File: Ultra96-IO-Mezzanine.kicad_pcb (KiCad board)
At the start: 2 copper layers, 85 x 54 mm, 6 parts, among them P1 CONN_02X20, P2 CONN_02X20

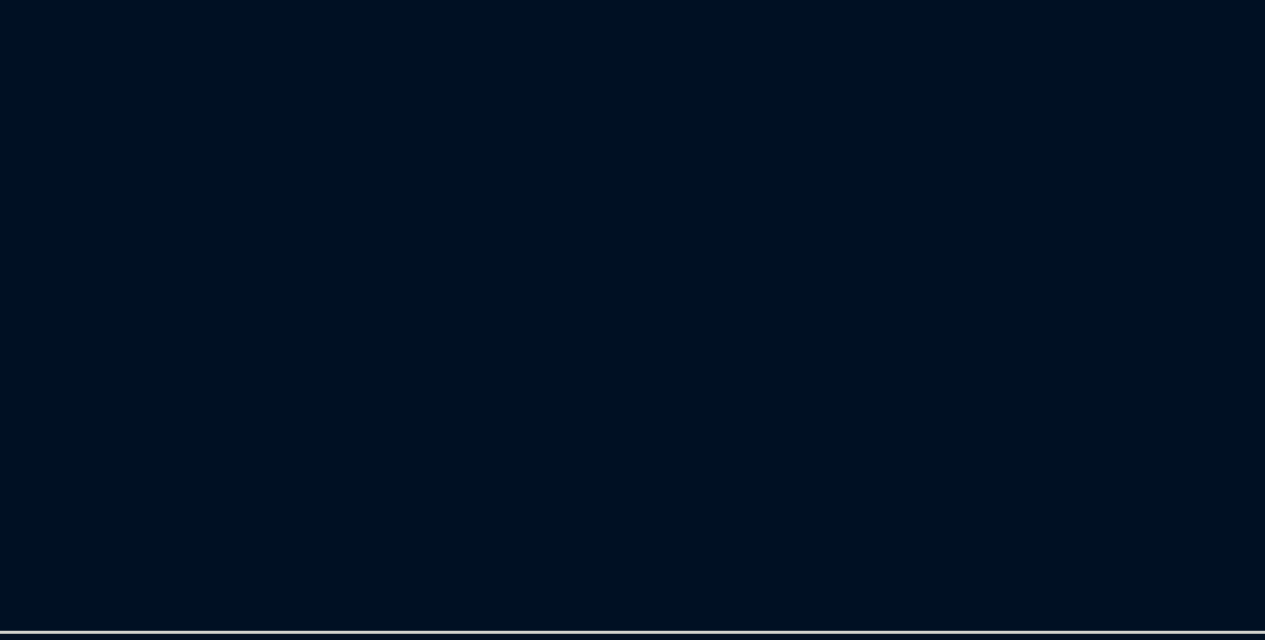
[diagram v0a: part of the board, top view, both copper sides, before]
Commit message: highspeed connector
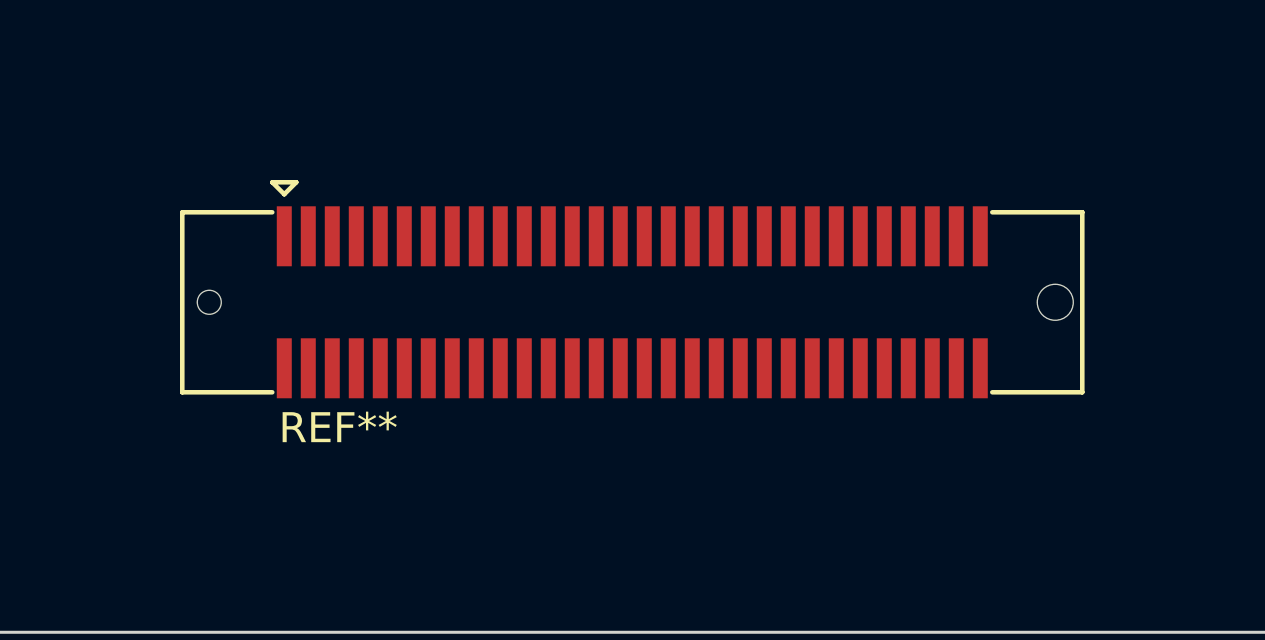
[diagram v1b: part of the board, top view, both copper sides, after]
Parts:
- added REF**: 61083-063400LF, 96board-hs:61083-063400LF, F.Cu at (130.8, 143.0)
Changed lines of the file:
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@@
-(kicad_pcb (version 20171130) (host pcbnew 5.1.6-c6e7f7d~86~ubuntu20.04.1)
+(kicad_pcb (version 20171130) (host pcbnew 5.1.6-c6e7f7d~87~ubuntu20.04.1)
   (general
     (thickness 1.6)
@@
     (tracks 0)
     (zones 0)
-    (modules 6)
+    (modules 7)
     (nets 37)
   )
@@
     (add_net GND)
   )
+  (module 96board-hs:61083-063400LF (layer F.Cu)
+    (at 130.8 143)
+    (fp_text reference REF** (at -9.8 4.2) (layer F.SilkS)
+      (effects (font (size 1 1) (thickness 0.15)))
+    )
+    (fp_text value 61083-063400LF (at -0.2 0) (layer F.Fab)
+      (effects (font (size 1 1) (thickness 0.15)))
+    )
+    (fp_line (start -15 -3) (end -15 3) (layer F.SilkS) (width 0.1524))
+    (fp_line (start 15 -3) (end 15 3) (layer F.SilkS) (width 0.1524))
+    (fp_line (start 15 -3) (end 12 -3) (layer F.SilkS) (width 0.1524))
+    (fp_line (start 15 3) (end 12 3) (layer F.SilkS) (width 0.1524))
+    (fp_line (start -15 3) (end -12 3) (layer F.SilkS) (width 0.1524))
+    (fp_line (start -15 -3) (end -12 -3) (layer F.SilkS) (width 0.1524))
+    (fp_line (start -12 -4) (end -11.6 -3.6) (layer F.SilkS) (width 0.1524))
+    (fp_line (start -11.6 -3.6) (end -11.2 -4) (layer F.SilkS) (width 0.1524))
+    (fp_line (start -11.2 -4) (end -12 -4) (layer F.SilkS) (width 0.1524))
+    (pad 57 smd rect (at 10.8 -2.2) (size 0.5 2) (layers F.Cu F.Paste F.Mask))
+    (pad 54 smd rect (at 9.2 2.2) (size 0.5 2) (layers F.Cu F.Paste F.Mask))
+    (pad 34 smd rect (at 1.2 2.2) (size 0.5 2) (layers F.Cu F.Paste F.Mask))
+    (pad 44 smd rect (at 5.2 2.2) (size 0.5 2) (layers F.Cu F.Paste F.Mask))
+    (pad 43 smd rect (at 5.2 -2.2) (size 0.5 2) (layers F.Cu F.Paste F.Mask))
+    (pad 39 smd rect (at 3.6 -2.2) (size 0.5 2) (layers F.Cu F.Paste F.Mask))
+    (pad 32 smd rect (at 0.4 2.2) (size 0.5 2) (layers F.Cu F.Paste F.Mask))
+    (pad 42 smd rect (at 4.4 2.2) (size 0.5 2) (layers F.Cu F.Paste F.Mask))
+    (pad 40 smd rect (at 3.6 2.2) (size 0.5 2) (layers F.Cu F.Paste F.Mask))
+    (pad 48 smd rect (at 6.8 2.2) (size 0.5 2) (layers F.Cu F.Paste F.Mask))
+    (pad 33 smd rect (at 1.2 -2.2) (size 0.5 2) (layers F.Cu F.Paste F.Mask))
+    (pad 51 smd rect (at 8.4 -2.2) (size 0.5 2) (layers F.Cu F.Paste F.Mask))
+    (pad 41 smd rect (at 4.4 -2.2) (size 0.5 2) (layers F.Cu F.Paste F.Mask))
+    (pad 37 smd rect (at 2.8 -2.2) (size 0.5 2) (layers F.Cu F.Paste F.Mask))
+    (pad 53 smd rect (at 9.2 -2.2) (size 0.5 2) (layers F.Cu F.Paste F.Mask))
+    (pad 35 smd rect (at 2 -2.2) (size 0.5 2) (layers F.Cu F.Paste F.Mask))
+    (pad 38 smd rect (at 2.8 2.2) (size 0.5 2) (layers F.Cu F.Paste F.Mask))
+    (pad 31 smd rect (at 0.4 -2.2) (size 0.5 2) (layers F.Cu F.Paste F.Mask))
+    (pad 58 smd rect (at 10.8 2.2) (size 0.5 2) (layers F.Cu F.Paste F.Mask))
+    (pad 55 smd rect (at 10 -2.2) (size 0.5 2) (layers F.Cu F.Paste F.Mask))
+    (pad 46 smd rect (at 6 2.2) (size 0.5 2) (layers F.Cu F.Paste F.Mask))
+    (pad 45 smd rect (at 6 -2.2) (size 0.5 2) (layers F.Cu F.Paste F.Mask))
+    (pad 49 smd rect (at 7.6 -2.2) (size 0.5 2) (layers F.Cu F.Paste F.Mask))
+    (pad 52 smd rect (at 8.4 2.2) (size 0.5 2) (layers F.Cu F.Paste F.Mask))
+    (pad 60 smd rect (at 11.6 2.2) (size 0.5 2) (layers F.Cu F.Paste F.Mask))
+    (pad 56 smd rect (at 10 2.2) (size 0.5 2) (layers F.Cu F.Paste F.Mask))
+    (pad 50 smd rect (at 7.6 2.2) (size 0.5 2) (layers F.Cu F.Paste F.Mask))
+    (pad 36 smd rect (at 2 2.2) (size 0.5 2) (layers F.Cu F.Paste F.Mask))
+    (pad 59 smd rect (at 11.6 -2.2) (size 0.5 2) (layers F.Cu F.Paste F.Mask))
+    (pad 47 smd rect (at 6.8 -2.2) (size 0.5 2) (layers F.Cu F.Paste F.Mask))
+    (pad "" np_thru_hole circle (at 14.1 0) (size 1.2 1.2) (drill 1.2) (layers *.Cu *.Mask))
+    (pad 1 smd rect (at -11.6 -2.2) (size 0.5 2) (layers F.Cu F.Paste F.Mask))
+    (pad 2 smd rect (at -11.6 2.2) (size 0.5 2) (layers F.Cu F.Paste F.Mask))
+    (pad 4 smd rect (at -10.8 2.2) (size 0.5 2) (layers F.Cu F.Paste F.Mask))
+    (pad 3 smd rect (at -10.8 -2.2) (size 0.5 2) (layers F.Cu F.Paste F.Mask))
+    (pad 6 smd rect (at -10 2.2) (size 0.5 2) (layers F.Cu F.Paste F.Mask))
+    (pad 5 smd rect (at -10 -2.2) (size 0.5 2) (layers F.Cu F.Paste F.Mask))
+    (pad 8 smd rect (at -9.2 2.2) (size 0.5 2) (layers F.Cu F.Paste F.Mask))
+    (pad 7 smd rect (at -9.2 -2.2) (size 0.5 2) (layers F.Cu F.Paste F.Mask))
+    (pad 9 smd rect (at -8.4 -2.2) (size 0.5 2) (layers F.Cu F.Paste F.Mask))
+    (pad 10 smd rect (at -8.4 2.2) (size 0.5 2) (layers F.Cu F.Paste F.Mask))
+    (pad 11 smd rect (at -7.6 -2.2) (size 0.5 2) (layers F.Cu F.Paste F.Mask))
+    (pad 12 smd rect (at -7.6 2.2) (size 0.5 2) (layers F.Cu F.Paste F.Mask))
+    (pad 13 smd rect (at -6.8 -2.2) (size 0.5 2) (layers F.Cu F.Paste F.Mask))
+    (pad 14 smd rect (at -6.8 2.2) (size 0.5 2) (layers F.Cu F.Paste F.Mask))
+    (pad 15 smd rect (at -6 -2.2) (size 0.5 2) (layers F.Cu F.Paste F.Mask))
+    (pad 16 smd rect (at -6 2.2) (size 0.5 2) (layers F.Cu F.Paste F.Mask))
+    (pad 18 smd rect (at -5.2 2.2) (size 0.5 2) (layers F.Cu F.Paste F.Mask))
+    (pad 17 smd rect (at -5.2 -2.2) (size 0.5 2) (layers F.Cu F.Paste F.Mask))
+    (pad 20 smd rect (at -4.4 2.2) (size 0.5 2) (layers F.Cu F.Paste F.Mask))
+    (pad 19 smd rect (at -4.4 -2.2) (size 0.5 2) (layers F.Cu F.Paste F.Mask))
+    (pad 21 smd rect (at -3.6 -2.2) (size 0.5 2) (layers F.Cu F.Paste F.Mask))
+    (pad 22 smd rect (at -3.6 2.2) (size 0.5 2) (layers F.Cu F.Paste F.Mask))
+    (pad 23 smd rect (at -2.8 -2.2) (size 0.5 2) (layers F.Cu F.Paste F.Mask))
+    (pad 24 smd rect (at -2.8 2.2) (size 0.5 2) (layers F.Cu F.Paste F.Mask))
+    (pad 26 smd rect (at -2 2.2) (size 0.5 2) (layers F.Cu F.Paste F.Mask))
+    (pad 25 smd rect (at -2 -2.2) (size 0.5 2) (layers F.Cu F.Paste F.Mask))
+    (pad 29 smd rect (at -0.4 -2.2) (size 0.5 2) (layers F.Cu F.Paste F.Mask))
+    (pad 30 smd rect (at -0.4 2.2) (size 0.5 2) (layers F.Cu F.Paste F.Mask))
+    (pad 28 smd rect (at -1.2 2.2) (size 0.5 2) (layers F.Cu F.Paste F.Mask))
+    (pad 27 smd rect (at -1.2 -2.2) (size 0.5 2) (layers F.Cu F.Paste F.Mask))
+    (pad "" np_thru_hole circle (at -14.1 0) (size 0.8 0.8) (drill 0.8) (layers *.Cu *.Mask))
+    (model ${KIPRJMOD}/96boards.pretty/61083-063400LF.wrl
+      (at (xyz 0 0 0))
+      (scale (xyz 0.394 0.394 0.394))
+      (rotate (xyz -90 0 0))
+    )
+  )
   (module 96boards:Socket_Strip_Straight_2x20_Pitch2mm locked (layer F.Cu)
     (at 110 105 90)
@@
       (effects (font (size 1.016 1.016) (thickness 0.2032)))
     )
+    (fp_line (start 1 -1) (end 1 1) (layer F.SilkS) (width 0.15))
+    (fp_line (start 3 -1) (end 1 -1) (layer F.SilkS) (width 0.15))
+    (fp_line (start 3 39) (end 3 -1) (layer F.SilkS) (width 0.15))
+    (fp_line (start -1 39) (end 3 39) (layer F.SilkS) (width 0.15))
+    (fp_line (start -1 1) (end -1 39) (layer F.SilkS) (width 0.15))
+    (fp_line (start 1 1) (end -1 1) (layer F.SilkS) (width 0.15))
+    (fp_line (start -1.5 -1.5) (end 3.5 -1.5) (layer F.CrtYd) (width 0.15))
+    (fp_line (start -1.5 39.5) (end -1.5 -1.5) (layer F.CrtYd) (width 0.15))
+    (fp_line (start 3.5 39.5) (end -1.5 39.5) (layer F.CrtYd) (width 0.15))
+    (fp_line (start 3.5 -1.5) (end 3.5 39.5) (layer F.CrtYd) (width 0.15))
+    (fp_line (start -1.2 -1.2) (end -1.2 0) (layer F.SilkS) (width 0.15))
     (fp_line (start 0 -1.2) (end -1.2 -1.2) (layer F.SilkS) (width 0.15))
-    (fp_line (start -1.2 -1.2) (end -1.2 0) (layer F.SilkS) (width 0.15))
-    (fp_line (start 3.5 -1.5) (end 3.5 39.5) (layer F.CrtYd) (width 0.15))
-    (fp_line (start 3.5 39.5) (end -1.5 39.5) (layer F.CrtYd) (width 0.15))
-    (fp_line (start -1.5 39.5) (end -1.5 -1.5) (layer F.CrtYd) (width 0.15))
-    (fp_line (start -1.5 -1.5) (end 3.5 -1.5) (layer F.CrtYd) (width 0.15))
-    (fp_line (start 1 1) (end -1 1) (layer F.SilkS) (width 0.15))
-    (fp_line (start -1 1) (end -1 39) (layer F.SilkS) (width 0.15))
-    (fp_line (start -1 39) (end 3 39) (layer F.SilkS) (width 0.15))
-    (fp_line (start 3 39) (end 3 -1) (layer F.SilkS) (width 0.15))
-    (fp_line (start 3 -1) (end 1 -1) (layer F.SilkS) (width 0.15))
-    (fp_line (start 1 -1) (end 1 1) (layer F.SilkS) (width 0.15))
     (pad 40 thru_hole circle (at 2 38) (size 1.2 1.2) (drill 0.8) (layers *.Cu *.Mask F.SilkS)
       (net 2 GND))
@@
       (effects (font (size 1.016 1.016) (thickness 0.2032)) (justify mirror))
     )
+    (fp_line (start -4.95 0.6) (end -4.95 -38.7) (layer B.SilkS) (width 0.15))
+    (fp_line (start -4.95 -38.7) (end 2.95 -38.7) (layer B.SilkS) (width 0.15))
+    (fp_line (start -4.95 0.6) (end 2.95 0.6) (layer B.SilkS) (width 0.15))
     (fp_line (start 2.95 0.6) (end 2.95 -38.7) (layer B.SilkS) (width 0.15))
-    (fp_line (start -4.95 0.6) (end 2.95 0.6) (layer B.SilkS) (width 0.15))
-    (fp_line (start -4.95 -38.7) (end 2.95 -38.7) (layer B.SilkS) (width 0.15))
-    (fp_line (start -4.95 0.6) (end -4.95 -38.7) (layer B.SilkS) (width 0.15))
     (pad "" np_thru_hole circle (at -1 -37) (size 1.2 1.2) (drill 1.2) (layers *.Cu *.Mask B.SilkS))
     (pad 1 smd rect (at 1.25 0) (size 0.89 3) (layers B.Cu B.Paste B.Mask)
